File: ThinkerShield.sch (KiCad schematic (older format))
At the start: 34 parts, among them SW1 SW_PUSHBUTTON, SW2 SW_PUSHBUTTON, U1 BUZZER

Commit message: Remove WS2812B LEDs, add sixth green LED for D13
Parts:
- removed C1: 100nF, FT:0603_CAP, symbol C
- removed LED6, LED7: WS2812B, FT:WS2812B, symbol WS2812B
- added LED6: GREEN, FT:LED-0805, symbol LED
- added R6: 470R, FT:0603, symbol R
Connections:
- wire segments 119 -> 111
- no-connect marks 14 -> 13
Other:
- note removed: "RGB LEDs - WS2812B"
- moved on the sheet: JP1, JP10, JP11, JP12, JP13, JP2, JP3, JP4, JP5, JP6, JP7, JP8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

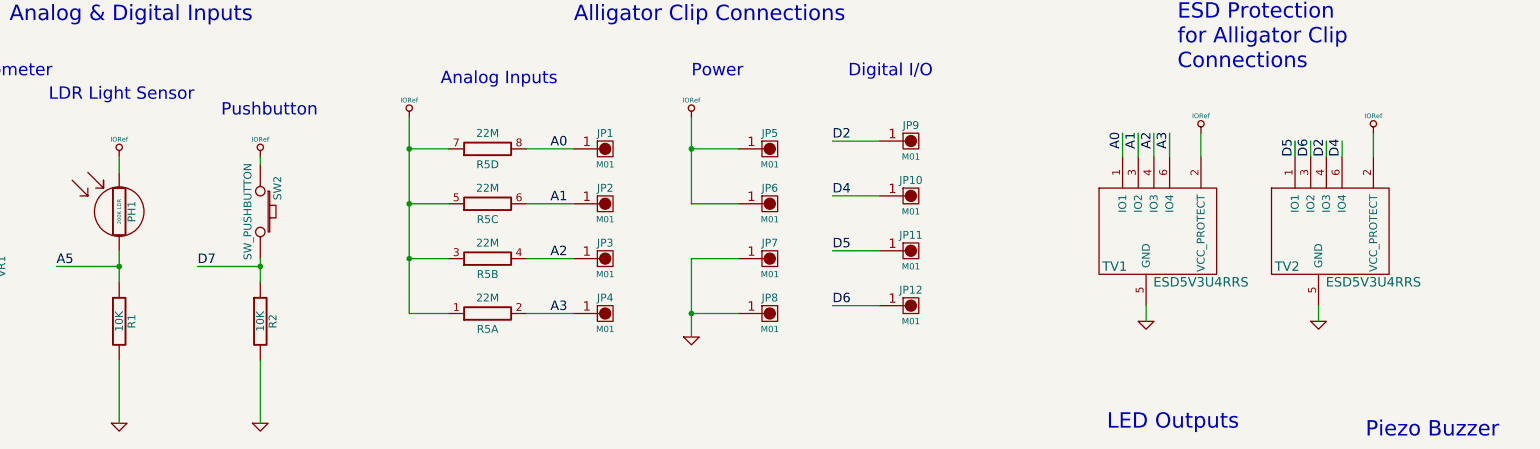
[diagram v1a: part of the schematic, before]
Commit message: Swap TVDS to SMF05C, swap 22M resistors to individual, add body outline around RV09
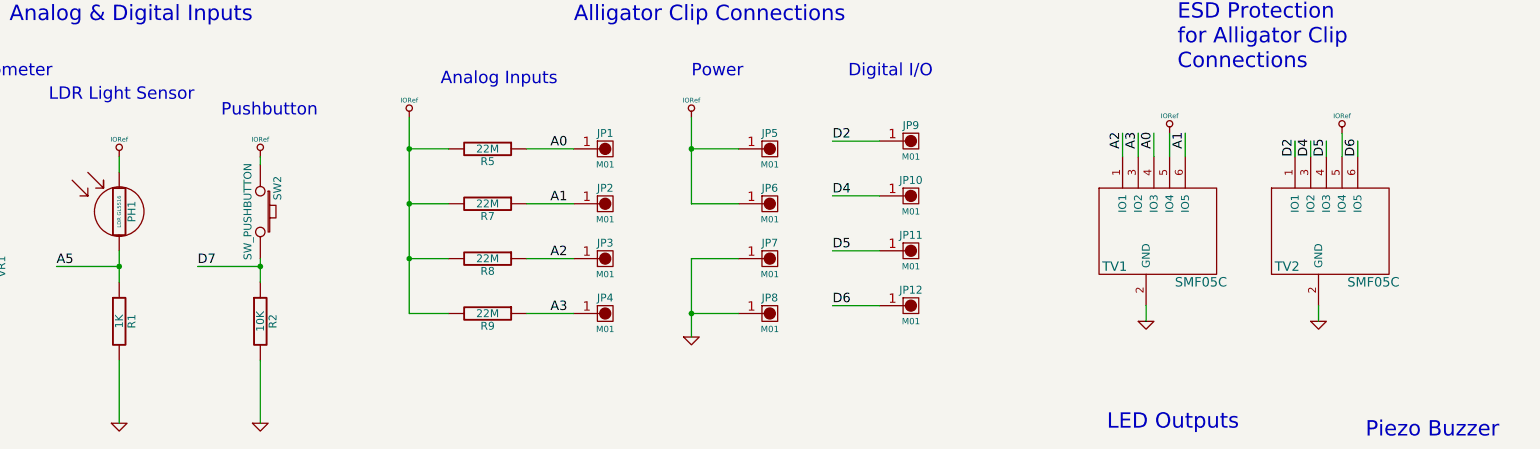
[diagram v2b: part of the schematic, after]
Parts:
- removed R5: 22M, FT:RES_CAY16, symbol R_PACK4_IND
- removed TV1, TV2: ESD5V3U4RRS, FT:SOT363, symbol ESD5V3U4RRS
- added R5, R7, R8, R9: 22M, FT:0603, symbol R
- added TV1, TV2: SMF05C, FT:SOT363, symbol SMF05C
- PH1: value 200K LDR -> LDR GL5516
- R1: value 10K -> 1K
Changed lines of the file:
@@
 P 2150 2150
 F 0 "PH1" V 2230 2150 50  0000 C CNN
-F 1 "200K LDR" V 2150 2150 24  0000 C CNN
+F 1 "LDR GL5516" V 2150 2150 24  0000 C CNN
 F 2 "FT:1X02" H 2150 2150 60  0001 C CNN
 F 3 "" H 2150 2150 60  0000 C CNN
@@
 P 2150 2850
 F 0 "R1" V 2230 2850 50  0000 C CNN
-F 1 "10K" V 2150 2850 50  0000 C CNN
+F 1 "1K" V 2150 2850 50  0000 C CNN
 F 2 "FT:0603" H 2150 2850 60  0001 C CNN
 F 3 "" H 2150 2850 60  0000 C CNN
@@
 F 3 "" H 5350 2800 60  0000 C CNN
 	1    5350 2800
-	1    0    0    -1
-$EndComp
-$Comp
-L R_PACK4_IND R5
-U 4 1 54891843
-P 4500 1750
-F 0 "R5" H 4500 1650 50  0000 C CNN
-F 1 "22M" H 4500 1850 50  0000 C CNN
-F 2 "FT:RES_CAY16" H 4500 1600 39  0001 C CNN
-F 3 "" H 4500 1750 60  0000 C CNN
-	4    4500 1750
-	1    0    0    -1
-$EndComp
-$Comp
-L R_PACK4_IND R5
-U 3 1 5489198D
-P 4500 2100
-F 0 "R5" H 4500 2000 50  0000 C CNN
-F 1 "22M" H 4500 2200 50  0000 C CNN
-F 2 "FT:RES_CAY16" H 4500 1950 39  0001 C CNN
-F 3 "" H 4500 2100 60  0000 C CNN
-	3    4500 2100
-	1    0    0    -1
-$EndComp
-$Comp
-L R_PACK4_IND R5
-U 2 1 548919C5
-P 4500 2450
-F 0 "R5" H 4500 2350 50  0000 C CNN
-F 1 "22M" H 4500 2550 50  0000 C CNN
-F 2 "FT:RES_CAY16" H 4500 2300 39  0001 C CNN
-F 3 "" H 4500 2450 60  0000 C CNN
-	2    4500 2450
-	1    0    0    -1
-$EndComp
-$Comp
-L R_PACK4_IND R5
-U 1 1 54891A04
-P 4500 2800
-F 0 "R5" H 4500 2700 50  0000 C CNN
-F 1 "22M" H 4500 2900 50  0000 C CNN
-F 2 "FT:RES_CAY16" H 4500 2650 39  0001 C CNN
-F 3 "" H 4500 2800 60  0000 C CNN
-	1    4500 2800
 	1    0    0    -1
 $EndComp
@@
 	0    1    1    0
 $EndComp
-$Comp
-L ESD5V3U4RRS TV1
-U 1 1 548A69AB
-P 8750 2250
-F 0 "TV1" H 8500 2000 60  0000 C CNN
-F 1 "ESD5V3U4RRS" H 9050 1900 60  0000 C CNN
-F 2 "FT:SOT363" H 9050 2000 60  0001 C CNN
-F 3 "" H 9050 2000 60  0000 C CNN
-	1    8750 2250
-	1    0    0    -1
-$EndComp
-$Comp
-L ESD5V3U4RRS TV2
-U 1 1 548A6A22
-P 9850 2250
-F 0 "TV2" H 9600 2000 60  0000 C CNN
-F 1 "ESD5V3U4RRS" H 10150 1900 60  0000 C CNN
-F 2 "FT:SOT363" H 10150 2000 60  0001 C CNN
-F 3 "" H 10150 2000 60  0000 C CNN
-	1    9850 2250
-	1    0    0    -1
-$EndComp
 Wire Wire Line
 	8700 2750 8700 2850
@@
 	9800 2850 9800 2750
 Wire Wire Line
-	10150 1650 10150 1800
+	9950 1650 9950 1800
 $Comp
 L IORef #PWR019
 U 1 1 548A76AC
-P 10150 1650
-F 0 "#PWR019" H 10150 1610 30  0001 C CNN
-F 1 "IORef" H 10150 1760 30  0000 C CNN
-F 2 "" H 10150 1650 60  0000 C CNN
-F 3 "" H 10150 1650 60  0000 C CNN
-	1    10150 1650
-	1    0    0    -1
-$EndComp
+P 9950 1650
+F 0 "#PWR019" H 9950 1610 30  0001 C CNN
+F 1 "IORef" H 9950 1760 30  0000 C CNN
+F 2 "" H 9950 1650 60  0000 C CNN
+F 3 "" H 9950 1650 60  0000 C CNN
+	1    9950 1650
+	1    0    0    -1
+$EndComp
+Wire Wire Line
+	8950 1800 8950 1650
 Wire Wire Line
 	8850 1800 8850 1650
@@
 	8750 1800 8750 1650
 Wire Wire Line
-	8650 1800 8650 1650
-Wire Wire Line
 	8550 1800 8550 1650
+Text Label 8750 1750 1    60   ~ 0
+A0
+Text Label 8950 1750 1    60   ~ 0
+A1
 Text Label 8550 1750 1    60   ~ 0
-A0
+A2
 Text Label 8650 1750 1    60   ~ 0
-A1
-Text Label 8750 1750 1    60   ~ 0
-A2
-Text Label 8850 1750 1    60   ~ 0
 A3
 Wire Wire Line
+	9750 1800 9750 1700
+Wire Wire Line
+	10050 1800 10050 1700
+Wire Wire Line
+	9850 1800 9850 1700
+Wire Wire Line
 	9650 1800 9650 1700
-Wire Wire Line
-	9750 1800 9750 1700
-Wire Wire Line
-	9850 1800 9850 1700
-Wire Wire Line
-	9950 1800 9950 1700
+Text Label 9650 1800 1    60   ~ 0
+D2
+Text Label 9750 1800 1    60   ~ 0
+D4
 Text Label 9850 1800 1    60   ~ 0
-D2
-Text Label 9950 1800 1    60   ~ 0
-D4
-Text Label 9650 1800 1    60   ~ 0
 D5
-Text Label 9750 1800 1    60   ~ 0
+Text Label 10050 1800 1    60   ~ 0
 D6
 Text Notes 8900 1250 0    98   ~ 0
 ESD Protection\nfor Alligator Clip\nConnections
 Wire Wire Line
-	9050 1650 9050 1800
+	8650 1650 8650 1800
 $Comp
 L IORef #PWR020
 U 1 1 548ABF15
-P 9050 1650
-F 0 "#PWR020" H 9050 1610 30  0001 C CNN
-F 1 "IORef" H 9050 1760 30  0000 C CNN
-F 2 "" H 9050 1650 60  0000 C CNN
-F 3 "" H 9050 1650 60  0000 C CNN
-	1    9050 1650
+P 8850 1650
+F 0 "#PWR020" H 8850 1610 30  0001 C CNN
+F 1 "IORef" H 8850 1760 30  0000 C CNN
+F 2 "" H 8850 1650 60  0000 C CNN
+F 3 "" H 8850 1650 60  0000 C CNN
+	1    8850 1650
 	1    0    0    -1
 $EndComp
@@
 	9500 5800 9650 5800
 Connection ~ 9650 5800
+$Comp
+L R R5
+U 1 1 555C3BC2
+P 4500 1750
+F 0 "R5" V 4580 1750 50  0000 C CNN
+F 1 "22M" V 4500 1750 50  0000 C CNN
+F 2 "FT:0603" H 4500 1750 60  0001 C CNN
+F 3 "" H 4500 1750 60  0000 C CNN
+	1    4500 1750
+	0    1    1    0
+$EndComp
+$Comp
+L R R7
+U 1 1 555C3CBC
+P 4500 2100
+F 0 "R7" V 4580 2100 50  0000 C CNN
+F 1 "22M" V 4500 2100 50  0000 C CNN
+F 2 "FT:0603" H 4500 2100 60  0001 C CNN
+F 3 "" H 4500 2100 60  0000 C CNN
+	1    4500 2100
+	0    1    1    0
+$EndComp
+$Comp
+L R R8
+U 1 1 555C3D2E
+P 4500 2450
+F 0 "R8" V 4580 2450 50  0000 C CNN
+F 1 "22M" V 4500 2450 50  0000 C CNN
+F 2 "FT:0603" H 4500 2450 60  0001 C CNN
+F 3 "" H 4500 2450 60  0000 C CNN
+	1    4500 2450
+	0    1    1    0
+$EndComp
+$Comp
+L R R9
+U 1 1 555C3DF8
+P 4500 2800
+F 0 "R9" V 4580 2800 50  0000 C CNN
+F 1 "22M" V 4500 2800 50  0000 C CNN
+F 2 "FT:0603" H 4500 2800 60  0001 C CNN
+F 3 "" H 4500 2800 60  0000 C CNN
+	1    4500 2800
+	0    1    1    0
+$EndComp
+$Comp
+L SMF05C TV1
+U 1 1 555C4E49
+P 8750 2250
+F 0 "TV1" H 8500 2000 60  0000 C CNN
+F 1 "SMF05C" H 9050 1900 60  0000 C CNN
+F 2 "FT:SOT363" H 9050 1800 60  0001 C CNN
+F 3 "" H 9050 2000 60  0000 C CNN
+	1    8750 2250
+	1    0    0    -1
+$EndComp
+$Comp
+L SMF05C TV2
+U 1 1 555C4EB6
+P 9850 2250
+F 0 "TV2" H 9600 2000 60  0000 C CNN
+F 1 "SMF05C" H 10150 1900 60  0000 C CNN
+F 2 "FT:SOT363" H 10150 1800 60  0001 C CNN
+F 3 "" H 10150 2000 60  0000 C CNN
+	1    9850 2250
+	1    0    0    -1
+$EndComp
 $EndSCHEMATC

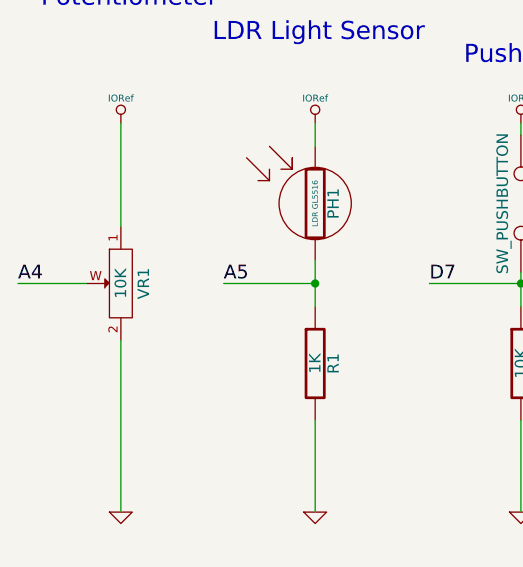
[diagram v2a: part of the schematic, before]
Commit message: Swap pot orientation so CCW = min value
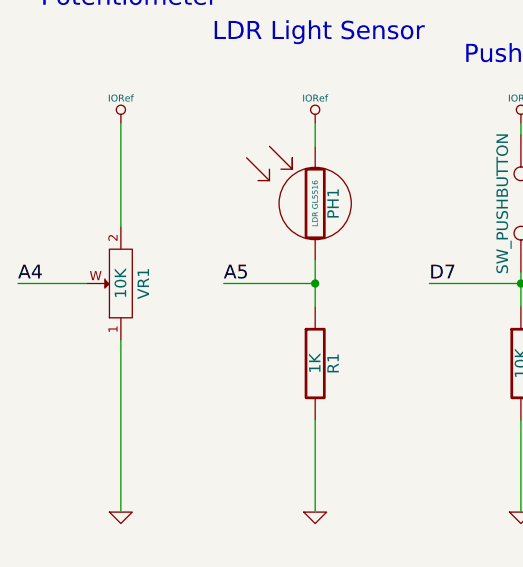
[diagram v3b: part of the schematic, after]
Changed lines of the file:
@@
 F 3 "" H 1300 2500 60  0000 C CNN
 	1    1300 2500
-	0    -1   1    0
+	0    -1   -1   0
 $EndComp
 $Comp

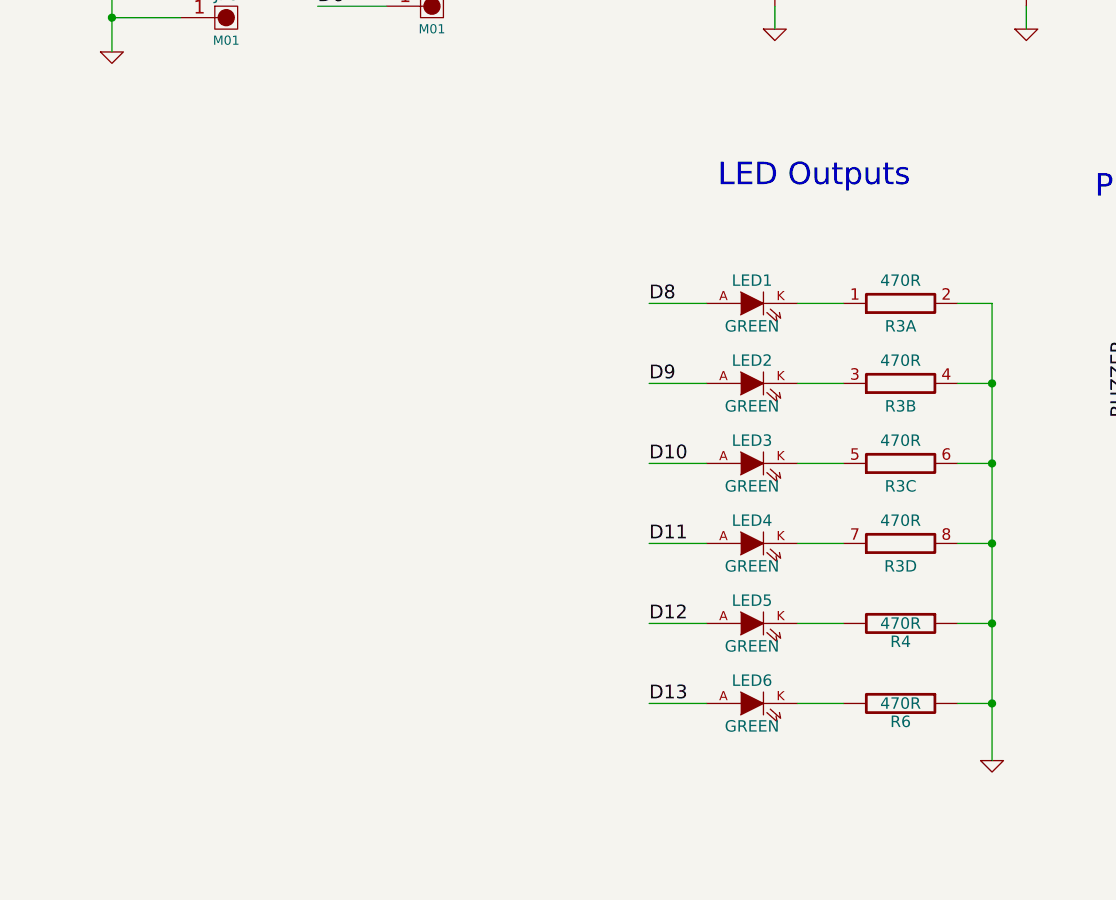
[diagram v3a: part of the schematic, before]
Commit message: Add power LED
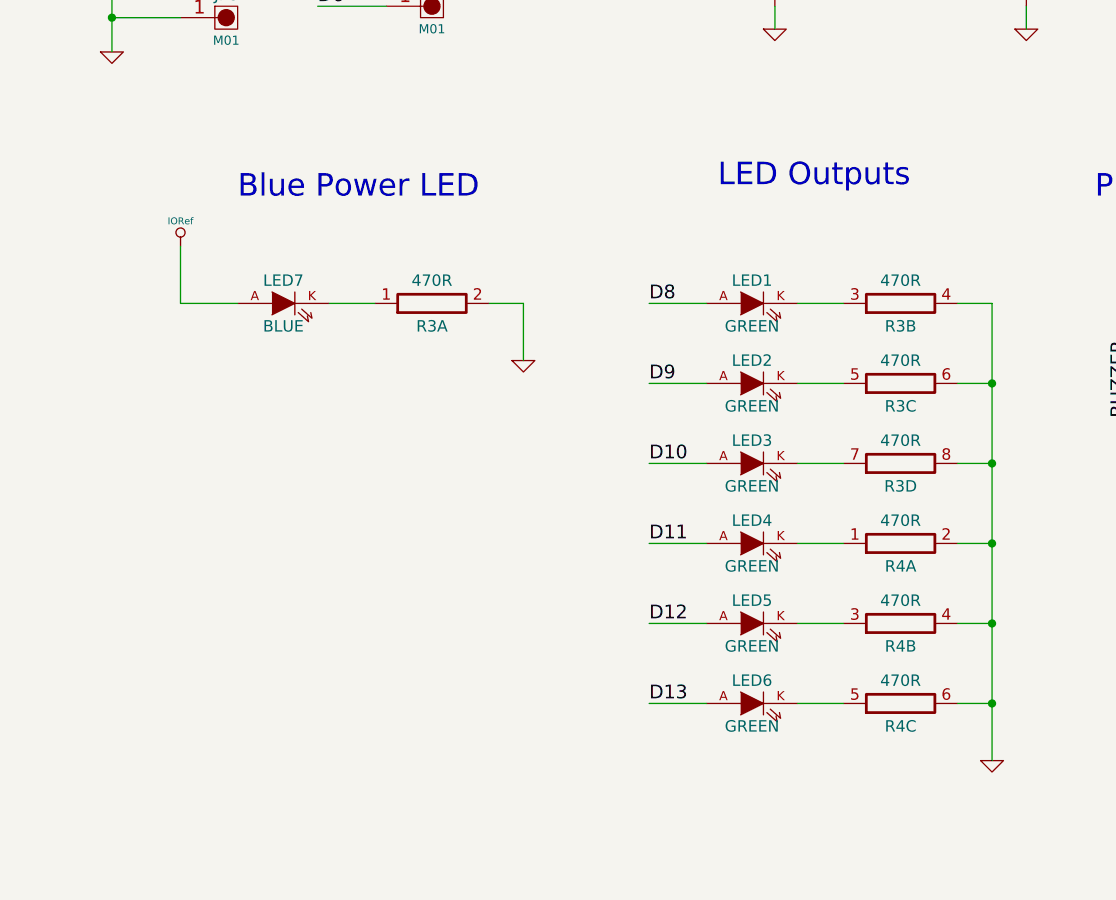
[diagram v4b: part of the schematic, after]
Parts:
- removed R4, R6: 470R, FT:0603, symbol R
- added LED7: BLUE, FT:LED-0805, symbol LED
- added unit 1 of R3
- added unit 2 of R4
- added unit 3 of R4
- renumbered R3 to R4
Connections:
- wire segments 111 -> 116
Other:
- note added: "Blue Power LED\n"
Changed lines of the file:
@@
 $Comp
 L R_PACK4_IND R3
-U 1 1 54895F4D
+U 2 1 54895F4D
 P 9250 4050
 F 0 "R3" H 9250 3950 50  0000 C CNN
@@
 F 2 "FT:RES_CAY16" H 9250 3900 39  0001 C CNN
 F 3 "" H 9250 4050 60  0000 C CNN
-	1    9250 4050
+	2    9250 4050
 	1    0    0    -1
 $EndComp
 $Comp
 L R_PACK4_IND R3
-U 2 1 54895FDF
+U 3 1 54895FDF
 P 9250 4400
 F 0 "R3" H 9250 4300 50  0000 C CNN
@@
 F 2 "FT:RES_CAY16" H 9250 4250 39  0001 C CNN
 F 3 "" H 9250 4400 60  0000 C CNN
-	2    9250 4400
+	3    9250 4400
 	1    0    0    -1
 $EndComp
 $Comp
 L R_PACK4_IND R3
-U 3 1 5489601F
+U 4 1 5489601F
 P 9250 4750
 F 0 "R3" H 9250 4650 50  0000 C CNN
@@
 F 2 "FT:RES_CAY16" H 9250 4600 39  0001 C CNN
 F 3 "" H 9250 4750 60  0000 C CNN
-	3    9250 4750
-	1    0    0    -1
-$EndComp
-$Comp
-L R_PACK4_IND R3
-U 4 1 54896064
+	4    9250 4750
+	1    0    0    -1
+$EndComp
+$Comp
+L R_PACK4_IND R4
+U 1 1 54896064
 P 9250 5100
-F 0 "R3" H 9250 5000 50  0000 C CNN
+F 0 "R4" H 9250 5000 50  0000 C CNN
 F 1 "470R" H 9250 5200 50  0000 C CNN
 F 2 "FT:RES_CAY16" H 9250 4950 39  0001 C CNN
 F 3 "" H 9250 5100 60  0000 C CNN
-	4    9250 5100
+	1    9250 5100
 	1    0    0    -1
 $EndComp
@@
 NoConn ~ 4450 7100
 NoConn ~ 4450 7200
-$Comp
-L R R4
-U 1 1 548A5541
-P 9250 5450
-F 0 "R4" V 9330 5450 50  0000 C CNN
-F 1 "470R" V 9250 5450 50  0000 C CNN
-F 2 "FT:0603" H 9250 5450 60  0001 C CNN
-F 3 "" H 9250 5450 60  0000 C CNN
-	1    9250 5450
-	0    1    1    0
-$EndComp
 Wire Wire Line
 	8700 2750 8700 2850
@@
 Wire Wire Line
 	8800 5800 9000 5800
-$Comp
-L R R6
-U 1 1 5547FE38
-P 9250 5800
-F 0 "R6" V 9330 5800 50  0000 C CNN
-F 1 "470R" V 9250 5800 50  0000 C CNN
-F 2 "FT:0603" H 9250 5800 60  0001 C CNN
-F 3 "" H 9250 5800 60  0000 C CNN
-	1    9250 5800
-	0    1    1    0
-$EndComp
 Wire Wire Line
 	9500 5800 9650 5800
@@
 	1    0    0    -1
 $EndComp
+$Comp
+L LED LED7
+U 1 1 556FBBBC
+P 6550 4050
+F 0 "LED7" H 6550 4150 50  0000 C CNN
+F 1 "BLUE" H 6550 3950 50  0000 C CNN
+F 2 "FT:LED-0805" H 6550 4050 60  0001 C CNN
+F 3 "" H 6550 4050 60  0000 C CNN
+	1    6550 4050
+	1    0    0    -1
+$EndComp
+Wire Wire Line
+	6350 4050 6100 4050
+Wire Wire Line
+	6750 4050 6950 4050
+Wire Wire Line
+	7450 4050 7600 4050
+$Comp
+L R_PACK4_IND R4
+U 2 1 556FC4AC
+P 9250 5450
+F 0 "R4" H 9250 5350 50  0000 C CNN
+F 1 "470R" H 9250 5550 50  0000 C CNN
+F 2 "FT:RES_CAY16" H 9250 5300 39  0001 C CNN
+F 3 "" H 9250 5450 60  0000 C CNN
+	2    9250 5450
+	1    0    0    -1
+$EndComp
+$Comp
+L R_PACK4_IND R4
+U 3 1 556FC554
+P 9250 5800
+F 0 "R4" H 9250 5700 50  0000 C CNN
+F 1 "470R" H 9250 5900 50  0000 C CNN
+F 2 "FT:RES_CAY16" H 9250 5650 39  0001 C CNN
+F 3 "" H 9250 5800 60  0000 C CNN
+	3    9250 5800
+	1    0    0    -1
+$EndComp
+$Comp
+L R_PACK4_IND R3
+U 1 1 556FC603
+P 7200 4050
+F 0 "R3" H 7200 3950 50  0000 C CNN
+F 1 "470R" H 7200 4150 50  0000 C CNN
+F 2 "FT:RES_CAY16" H 7200 3900 39  0001 C CNN
+F 3 "" H 7200 4050 60  0000 C CNN
+	1    7200 4050
+	1    0    0    -1
+$EndComp
+Wire Wire Line
+	6100 4050 6100 3800
+$Comp
+L IORef #PWR021
+U 1 1 556FE007
+P 6100 3800
+F 0 "#PWR021" H 6100 3760 30  0001 C CNN
+F 1 "IORef" H 6100 3910 30  0000 C CNN
+F 2 "" H 6100 3800 60  0000 C CNN
+F 3 "" H 6100 3800 60  0000 C CNN
+	1    6100 3800
+	1    0    0    -1
+$EndComp
+Wire Wire Line
+	7600 4050 7600 4300
+$Comp
+L GND #PWR022
+U 1 1 556FE611
+P 7600 4300
+F 0 "#PWR022" H 7600 4300 30  0001 C CNN
+F 1 "GND" H 7600 4230 30  0001 C CNN
+F 2 "" H 7600 4300 60  0000 C CNN
+F 3 "" H 7600 4300 60  0000 C CNN
+	1    7600 4300
+	1    0    0    -1
+$EndComp
+Text Notes 6350 3600 0    98   ~ 0
+Blue Power LED\n
 $EndSCHEMATC

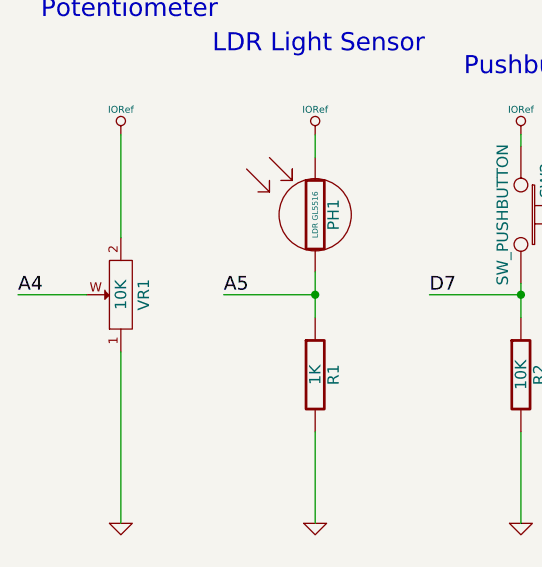
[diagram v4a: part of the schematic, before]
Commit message: Swap A4/A5 to be compatible with older Thinkup boards
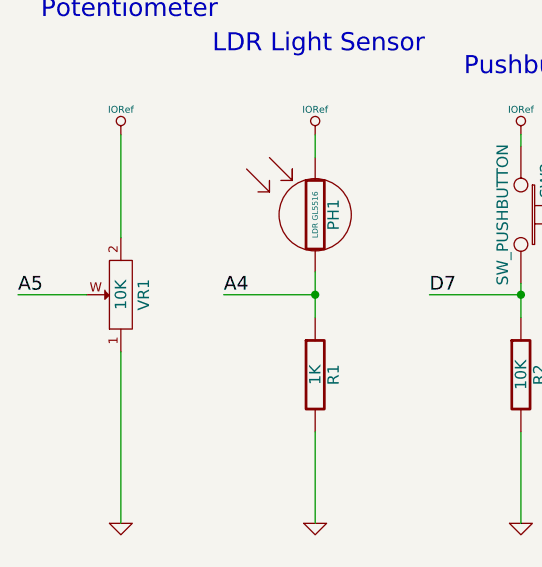
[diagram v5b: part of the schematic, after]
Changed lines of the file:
@@
 encoding utf-8
 Sheet 1 1
-Title ""
+Title "ThinkerShield"
 Date ""
-Rev ""
+Rev "V1.1"
 Comp ""
-Comment1 ""
+Comment1 "TAPR Open Hardware License"
 Comment2 ""
-Comment3 ""
+Comment3 "Copyright (C) 2015 Freetronics Pty Ltd"
 Comment4 ""
 $EndDescr
@@
 	1    0    0    -1
 $EndComp
-Text Label 1750 2500 0    60   ~ 0
+Text Label 850  2500 0    60   ~ 0
 A5
 $Comp
@@
 	1    0    0    -1
 $EndComp
-Text Label 850  2500 0    60   ~ 0
+Text Label 1750 2500 0    60   ~ 0
 A4
 $Comp
